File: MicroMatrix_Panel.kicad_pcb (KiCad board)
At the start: 2 copper layers, 86 x 36 mm, 385 parts

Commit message: Updated panel settings for fab
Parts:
- removed the REF** at (44.0, 43.2)
- removed the REF** at (49.4, 22.8)
- removed the REF** at (73.3, 43.2)
- removed the REF** at (66.0, 43.2)
- removed the REF** at (51.9, 43.2)
- removed the REF** at (20.0, 17.5) (x2)
- removed the REF** at (20.0, 48.5) (x2)
- removed the REF** at (96.0, 17.5) (x2)
- removed the REF** at (86.1, 22.8)
- removed the REF** at (66.0, 22.8)
- removed the REF** at (45.3, 22.8)
- removed the REF** at (89.3, 22.8)
- removed the REF** at (42.1, 22.8)
- removed the REF** at (71.4, 22.8)
- removed the REF** at (71.4, 43.2)
- removed the REF** at (94.7, 43.2)
- removed the REF** at (48.7, 43.2)
- removed the REF** at (44.6, 43.2)
- removed the REF** at (73.9, 43.2)
- removed the REF** at (28.0, 22.8)
- removed the REF** at (73.3, 22.8)
- removed the REF** at (27.4, 22.8)
- removed the REF** at (20.7, 43.2)
- removed the REF** at (42.7, 22.8)
- removed the REF** at (21.3, 43.2)
- removed the REF** at (22.6, 43.2)
- removed the REF** at (88.6, 43.2)
- removed the REF** at (42.7, 43.2)
- removed the REF** at (43.3, 43.2)
- removed the REF** at (45.3, 43.2)
- removed the REF** at (72.7, 22.8)
- removed the REF** at (44.6, 22.8)
- removed the REF** at (29.9, 22.8)
- removed the REF** at (64.7, 43.2)
- removed the REF** at (28.0, 43.2)
- removed the REF** at (51.3, 43.2)
- removed the REF** at (70.7, 43.2)
- removed the REF** at (67.3, 22.8)
- removed the REF** at (22.0, 43.2)
- removed the REF** at (28.7, 22.8)
- removed the REF** at (92.7, 22.8)
- removed the REF** at (67.3, 43.2)
- removed the REF** at (20.7, 22.8)
- removed the REF** at (22.0, 22.8)
- removed the REF** at (64.1, 22.8)
- removed the REF** at (26.7, 43.2)
- removed the REF** at (94.0, 22.8)
- removed the REF** at (88.6, 22.8)
- removed the REF** at (50.7, 43.2)
- removed the REF** at (95.9, 22.8)
- removed the REF** at (23.3, 43.2)
- removed the REF** at (64.1, 43.2)
- removed the REF** at (86.7, 43.2)
- removed the REF** at (28.7, 43.2)
- removed the REF** at (65.3, 22.8)
- removed the REF** at (20.1, 22.8)
- removed the REF** at (64.7, 22.8)
- removed the REF** at (95.9, 43.2)
- removed the REF** at (27.4, 43.2)
- removed the REF** at (66.6, 43.2)
- removed the REF** at (49.4, 43.2)
- removed the REF** at (23.3, 22.8)
- removed the REF** at (88.0, 22.8)
- removed the REF** at (93.4, 22.8)
- removed the REF** at (72.0, 22.8)
- removed the REF** at (29.9, 43.2)
- removed the REF** at (92.7, 43.2)
- removed the REF** at (50.0, 22.8)
- removed the REF** at (87.3, 43.2)
- removed the REF** at (51.3, 22.8)
- removed the REF** at (88.0, 43.2)
- removed the REF** at (87.3, 22.8)
- removed the REF** at (95.3, 22.8)
- removed the REF** at (29.3, 43.2)
- removed the REF** at (72.0, 43.2)
- removed the REF** at (95.3, 43.2)
- removed the REF** at (73.9, 22.8)
- removed the REF** at (66.6, 22.8)
- removed the REF** at (44.0, 22.8)
- removed the REF** at (70.7, 22.8)
- removed the REF** at (50.7, 22.8)
- removed the REF** at (22.6, 22.8)
- removed the REF** at (72.7, 43.2)
- removed the REF** at (86.7, 22.8)
- removed the REF** at (26.7, 22.8)
- removed the REF** at (20.1, 43.2)
- removed the REF** at (48.7, 22.8)
- removed the REF** at (42.1, 43.2)
- removed the REF** at (86.1, 43.2)
- removed the REF** at (51.9, 22.8)
- removed the REF** at (43.3, 22.8)
- removed the REF** at (94.7, 22.8)
- removed the REF** at (89.3, 43.2)
- removed the REF** at (65.3, 43.2)
- removed the REF** at (21.3, 22.8)
- removed the REF** at (29.3, 22.8)
- removed the REF** at (94.0, 43.2)
- removed the REF** at (93.4, 43.2)
- removed the REF** at (50.0, 43.2)
- added REF**: NPTH, NPTH, F.Cu at (95.8, 43.3)
- added REF**: Fiducial, Fiducial, F.Cu at (96.0, 17.5)
- added REF**: NPTH, NPTH, F.Cu at (95.8, 22.7)
- added REF**: NPTH, NPTH, F.Cu at (26.8, 22.7)
- added REF**: NPTH, NPTH, F.Cu at (49.8, 43.3)
- added REF**: NPTH, NPTH, F.Cu at (27.8, 22.7)
- added REF**: NPTH, NPTH, F.Cu at (94.8, 22.7)
- added REF**: NPTH, NPTH, F.Cu at (49.8, 22.7)
- added REF**: NPTH, NPTH, F.Cu at (66.2, 43.3)
- added REF**: NPTH, NPTH, F.Cu at (22.2, 43.3)
- added REF**: NPTH, NPTH, F.Cu at (71.8, 22.7)
- added REF**: NPTH, NPTH, F.Cu at (23.2, 43.3)
- added REF**: NPTH, NPTH, F.Cu at (65.2, 43.3)
- added REF**: NPTH, NPTH, F.Cu at (64.2, 43.3)
- added REF**: NPTH, NPTH, F.Cu at (86.2, 43.3)
- added REF**: NPTH, NPTH, F.Cu at (45.2, 43.3)
- added REF**: NPTH, NPTH, F.Cu at (23.2, 22.7)
- added REF**: NPTH, NPTH, F.Cu at (20.2, 22.7)
- added REF**: NPTH, NPTH, F.Cu at (73.8, 43.3)
- added REF**: NPTH, NPTH, F.Cu at (20.2, 43.3)
- added REF**: NPTH, NPTH, F.Cu at (89.2, 22.7)
- added REF**: NPTH, NPTH, F.Cu at (28.8, 43.3)
- added REF**: NPTH, NPTH, F.Cu at (44.2, 43.3)
- added REF**: NPTH, NPTH, F.Cu at (87.2, 43.3)
- added REF**: NPTH, NPTH, F.Cu at (72.8, 43.3)
- added REF**: NPTH, NPTH, F.Cu at (29.8, 22.7)
- added REF**: NPTH, NPTH, F.Cu at (88.2, 43.3)
- added REF**: NPTH, NPTH, F.Cu at (51.8, 22.7)
- added REF**: NPTH, NPTH, F.Cu at (50.8, 22.7)
- added REF**: NPTH, NPTH, F.Cu at (21.2, 43.3)
- added REF**: NPTH, NPTH, F.Cu at (92.8, 43.3)
- added REF**: NPTH, NPTH, F.Cu at (67.2, 43.3)
- added REF**: NPTH, NPTH, F.Cu at (93.8, 22.7)
- added REF**: NPTH, NPTH, F.Cu at (48.8, 43.3)
- added REF**: NPTH, NPTH, F.Cu at (65.2, 22.7)
- added REF**: NPTH, NPTH, F.Cu at (88.2, 22.7)
- added REF**: NPTH, NPTH, F.Cu at (64.2, 22.7)
- added REF**: NPTH, NPTH, F.Cu at (43.2, 43.3)
- added REF**: NPTH, NPTH, F.Cu at (45.2, 22.7)
- added REF**: NPTH, NPTH, F.Cu at (70.8, 22.7)
- added REF**: NPTH, NPTH, F.Cu at (48.8, 22.7)
- added REF**: NPTH, NPTH, F.Cu at (44.2, 22.7)
- added REF**: Fiducial, Fiducial, F.Cu at (20.0, 17.5)
- added REF**: NPTH, NPTH, F.Cu at (27.8, 43.3)
- added REF**: NPTH, NPTH, F.Cu at (28.8, 22.7)
- added REF**: NPTH, NPTH, F.Cu at (67.2, 22.7)
- added REF**: NPTH, NPTH, F.Cu at (22.2, 22.7)
- added REF**: Fiducial, Fiducial, F.Cu at (20.0, 48.5)
- added REF**: NPTH, NPTH, F.Cu at (86.2, 22.7)
- added REF**: NPTH, NPTH, F.Cu at (66.2, 22.7)
- added REF**: NPTH, NPTH, F.Cu at (94.8, 43.3)
- added REF**: NPTH, NPTH, F.Cu at (89.2, 43.3)
- added REF**: NPTH, NPTH, F.Cu at (50.8, 43.3)
- added REF**: NPTH, NPTH, F.Cu at (29.8, 43.3)
- added REF**: NPTH, NPTH, F.Cu at (42.2, 43.3)
- added REF**: NPTH, NPTH, F.Cu at (72.8, 22.7)
- added REF**: NPTH, NPTH, F.Cu at (71.8, 43.3)
- added REF**: NPTH, NPTH, F.Cu at (51.8, 43.3)
- added REF**: NPTH, NPTH, F.Cu at (42.2, 22.7)
- added REF**: NPTH, NPTH, F.Cu at (21.2, 22.7)
- added REF**: NPTH, NPTH, F.Cu at (93.8, 43.3)
- added REF**: NPTH, NPTH, F.Cu at (70.8, 43.3)
- added REF**: NPTH, NPTH, F.Cu at (87.2, 22.7)
- added REF**: NPTH, NPTH, F.Cu at (92.8, 22.7)
- added REF**: NPTH, NPTH, F.Cu at (43.2, 22.7)
- added REF**: Fiducial, Fiducial, B.Cu at (96.0, 17.5)
- added REF**: Fiducial, Fiducial, B.Cu at (20.0, 17.5)
- added REF**: Fiducial, Fiducial, B.Cu at (20.0, 48.5)
- added REF**: NPTH, NPTH, F.Cu at (26.8, 43.3)
- added REF**: NPTH, NPTH, F.Cu at (73.8, 22.7)
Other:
- outline, holes or cut-outs redrawn
- board text added: "JLCJLCJLCJLC - REV${REVISION} - ${ISSUE_DATE}"
- board text removed: "JLCJLCJLCJLC - ${REVISION} - ${ISSUE_DATE}"

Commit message: Updated Panel PCB to REV1.2
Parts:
- removed the D25 at (100.0, 31.4)
- removed the D25 at (56.0, 31.4)
- removed the D25 at (78.0, 31.4)
- removed the D25 at (34.0, 31.4)
- removed the D26 at (31.5, 31.4)
- removed the D26 at (53.5, 31.4)
- removed the D26 at (97.5, 31.4)
- removed the D26 at (75.5, 31.4)
- removed the D27 at (29.0, 31.4)
- removed the D27 at (95.0, 31.4)
- removed the D27 at (73.0, 31.4)
- removed the D27 at (51.0, 31.4)
- removed the D28 at (48.5, 31.4)
- removed the D28 at (26.5, 31.4)
- removed the D28 at (70.5, 31.4)
- removed the D28 at (92.5, 31.4)
- removed the D29 at (46.0, 31.4)
- removed the D29 at (24.0, 31.4)
- removed the D29 at (68.0, 31.4)
- removed the D29 at (90.0, 31.4)
- removed the D30 at (43.5, 31.4)
- removed the D30 at (21.5, 31.4)
- removed the D30 at (65.5, 31.4)
- removed the D30 at (87.5, 31.4)
- removed the D31 at (85.0, 31.4)
- removed the D31 at (19.0, 31.4)
- removed the D31 at (63.0, 31.4)
- removed the D31 at (41.0, 31.4)
- removed the D32 at (38.5, 31.4)
- removed the D32 at (60.5, 31.4)
- removed the D32 at (16.5, 31.4)
- removed the D32 at (82.5, 31.4)
- removed the REF** at (95.8, 43.3)
- removed the REF** at (96.0, 17.5) (x2)
- removed the REF** at (95.8, 22.7)
- removed the REF** at (26.8, 22.7)
- removed the REF** at (49.8, 43.3)
- removed the REF** at (27.8, 22.7)
- removed the REF** at (94.8, 22.7)
- removed the REF** at (49.8, 22.7)
- removed the REF** at (66.2, 43.3)
- removed the REF** at (22.2, 43.3)
- removed the REF** at (71.8, 22.7)
- removed the REF** at (23.2, 43.3)
- removed the REF** at (65.2, 43.3)
- removed the REF** at (64.2, 43.3)
- removed the REF** at (86.2, 43.3)
- removed the REF** at (45.2, 43.3)
- removed the REF** at (23.2, 22.7)
- removed the REF** at (20.2, 22.7)
- removed the REF** at (73.8, 43.3)
- removed the REF** at (20.2, 43.3)
- removed the REF** at (89.2, 22.7)
- removed the REF** at (28.8, 43.3)
- removed the REF** at (44.2, 43.3)
- removed the REF** at (87.2, 43.3)
- removed the REF** at (72.8, 43.3)
- removed the REF** at (29.8, 22.7)
- removed the REF** at (88.2, 43.3)
- removed the REF** at (51.8, 22.7)
- removed the REF** at (50.8, 22.7)
- removed the REF** at (21.2, 43.3)
- removed the REF** at (92.8, 43.3)
- removed the REF** at (67.2, 43.3)
- removed the REF** at (93.8, 22.7)
- removed the REF** at (48.8, 43.3)
- removed the REF** at (65.2, 22.7)
- removed the REF** at (88.2, 22.7)
- removed the REF** at (64.2, 22.7)
- removed the REF** at (43.2, 43.3)
- removed the REF** at (45.2, 22.7)
- removed the REF** at (70.8, 22.7)
- removed the REF** at (48.8, 22.7)
- removed the REF** at (44.2, 22.7)
- removed the REF** at (20.0, 17.5) (x2)
- removed the REF** at (27.8, 43.3)
- removed the REF** at (28.8, 22.7)
- removed the REF** at (67.2, 22.7)
- removed the REF** at (22.2, 22.7)
- removed the REF** at (20.0, 48.5) (x2)
- removed the REF** at (86.2, 22.7)
- removed the REF** at (66.2, 22.7)
- removed the REF** at (94.8, 43.3)
- removed the REF** at (89.2, 43.3)
- removed the REF** at (50.8, 43.3)
- removed the REF** at (29.8, 43.3)
- removed the REF** at (42.2, 43.3)
- removed the REF** at (72.8, 22.7)
- removed the REF** at (71.8, 43.3)
- removed the REF** at (51.8, 43.3)
- removed the REF** at (42.2, 22.7)
- removed the REF** at (21.2, 22.7)
- removed the REF** at (93.8, 43.3)
- removed the REF** at (70.8, 43.3)
- removed the REF** at (87.2, 22.7)
- removed the REF** at (92.8, 22.7)
- removed the REF** at (43.2, 22.7)
- removed the REF** at (26.8, 43.3)
- removed the REF** at (73.8, 22.7)
- added D25: SK6805, LED_SMD:LED_SK6812_EC15_1.5x1.5mm, F.Cu at (56.0, 31.5)
- added D25: SK6805, LED_SMD:LED_SK6812_EC15_1.5x1.5mm, F.Cu at (34.0, 31.5)
- added D25: SK6805, LED_SMD:LED_SK6812_EC15_1.5x1.5mm, F.Cu at (100.0, 31.5)
- added D25: SK6805, LED_SMD:LED_SK6812_EC15_1.5x1.5mm, F.Cu at (78.0, 31.5)
- added D26: SK6805, LED_SMD:LED_SK6812_EC15_1.5x1.5mm, F.Cu at (53.5, 31.5)
- added D26: SK6805, LED_SMD:LED_SK6812_EC15_1.5x1.5mm, F.Cu at (31.5, 31.5)
- added D26: SK6805, LED_SMD:LED_SK6812_EC15_1.5x1.5mm, F.Cu at (97.5, 31.5)
- added D26: SK6805, LED_SMD:LED_SK6812_EC15_1.5x1.5mm, F.Cu at (75.5, 31.5)
- added D27: SK6805, LED_SMD:LED_SK6812_EC15_1.5x1.5mm, F.Cu at (95.0, 31.5)
- added D27: SK6805, LED_SMD:LED_SK6812_EC15_1.5x1.5mm, F.Cu at (51.0, 31.5)
- added D27: SK6805, LED_SMD:LED_SK6812_EC15_1.5x1.5mm, F.Cu at (73.0, 31.5)
- added D27: SK6805, LED_SMD:LED_SK6812_EC15_1.5x1.5mm, F.Cu at (29.0, 31.5)
- added D28: SK6805, LED_SMD:LED_SK6812_EC15_1.5x1.5mm, F.Cu at (26.5, 31.5)
- added D28: SK6805, LED_SMD:LED_SK6812_EC15_1.5x1.5mm, F.Cu at (92.5, 31.5)
- added D28: SK6805, LED_SMD:LED_SK6812_EC15_1.5x1.5mm, F.Cu at (70.5, 31.5)
- added D28: SK6805, LED_SMD:LED_SK6812_EC15_1.5x1.5mm, F.Cu at (48.5, 31.5)
- added D29: SK6805, LED_SMD:LED_SK6812_EC15_1.5x1.5mm, F.Cu at (90.0, 31.5)
- added D29: SK6805, LED_SMD:LED_SK6812_EC15_1.5x1.5mm, F.Cu at (46.0, 31.5)
- added D29: SK6805, LED_SMD:LED_SK6812_EC15_1.5x1.5mm, F.Cu at (68.0, 31.5)
- added D29: SK6805, LED_SMD:LED_SK6812_EC15_1.5x1.5mm, F.Cu at (24.0, 31.5)
- added D30: SK6805, LED_SMD:LED_SK6812_EC15_1.5x1.5mm, F.Cu at (87.5, 31.5)
- added D30: SK6805, LED_SMD:LED_SK6812_EC15_1.5x1.5mm, F.Cu at (21.5, 31.5)
- added D30: SK6805, LED_SMD:LED_SK6812_EC15_1.5x1.5mm, F.Cu at (65.5, 31.5)
- added D30: SK6805, LED_SMD:LED_SK6812_EC15_1.5x1.5mm, F.Cu at (43.5, 31.5)
- added D31: SK6805, LED_SMD:LED_SK6812_EC15_1.5x1.5mm, F.Cu at (85.0, 31.5)
- added D31: SK6805, LED_SMD:LED_SK6812_EC15_1.5x1.5mm, F.Cu at (19.0, 31.5)
- added D31: SK6805, LED_SMD:LED_SK6812_EC15_1.5x1.5mm, F.Cu at (41.0, 31.5)
- added D31: SK6805, LED_SMD:LED_SK6812_EC15_1.5x1.5mm, F.Cu at (63.0, 31.5)
- added D32: SK6805, LED_SMD:LED_SK6812_EC15_1.5x1.5mm, F.Cu at (16.5, 31.5)
- added D32: SK6805, LED_SMD:LED_SK6812_EC15_1.5x1.5mm, F.Cu at (82.5, 31.5)
- added D32: SK6805, LED_SMD:LED_SK6812_EC15_1.5x1.5mm, F.Cu at (60.5, 31.5)
- added D32: SK6805, LED_SMD:LED_SK6812_EC15_1.5x1.5mm, F.Cu at (38.5, 31.5)
- added REF**: NPTH, NPTH, F.Cu at (67.5, 22.7)
- added REF**: NPTH, NPTH, F.Cu at (91.5, 43.3)
- added REF**: NPTH, NPTH, F.Cu at (25.5, 43.3)
- added REF**: NPTH, NPTH, F.Cu at (67.5, 43.3)
- added REF**: NPTH, NPTH, F.Cu at (70.5, 22.7)
- added REF**: NPTH, NPTH, F.Cu at (46.5, 43.3)
- added REF**: NPTH, NPTH, F.Cu at (92.5, 22.7)
- added REF**: NPTH, NPTH, F.Cu at (90.5, 22.7)
- added REF**: NPTH, NPTH, F.Cu at (45.5, 22.7)
- added REF**: NPTH, NPTH, F.Cu at (46.5, 22.7)
- added REF**: NPTH, NPTH, F.Cu at (24.5, 43.3)
- added REF**: NPTH, NPTH, F.Cu at (68.5, 43.3)
- added REF**: Fiducial, Fiducial, F.Cu at (96.0, 17.5)
- added REF**: NPTH, NPTH, F.Cu at (48.5, 22.7)
- added REF**: NPTH, NPTH, F.Cu at (70.5, 43.3)
- added REF**: NPTH, NPTH, F.Cu at (45.5, 43.3)
- added REF**: NPTH, NPTH, F.Cu at (47.5, 22.7)
- added REF**: NPTH, NPTH, F.Cu at (69.5, 22.7)
- added REF**: NPTH, NPTH, F.Cu at (47.5, 43.3)
- added REF**: NPTH, NPTH, F.Cu at (23.5, 22.7)
- added REF**: Fiducial, Fiducial, F.Cu at (20.0, 48.5)
- added REF**: NPTH, NPTH, F.Cu at (89.5, 22.7)
- added REF**: NPTH, NPTH, F.Cu at (48.5, 43.3)
- added REF**: NPTH, NPTH, F.Cu at (91.5, 22.7)
- added REF**: NPTH, NPTH, F.Cu at (24.5, 22.7)
- added REF**: NPTH, NPTH, F.Cu at (90.5, 43.3)
- added REF**: NPTH, NPTH, F.Cu at (89.5, 43.3)
- added REF**: NPTH, NPTH, F.Cu at (69.5, 43.3)
- added REF**: NPTH, NPTH, F.Cu at (25.5, 22.7)
- added REF**: Fiducial, Fiducial, B.Cu at (20.0, 48.5)
- added REF**: NPTH, NPTH, F.Cu at (92.5, 43.3)
- added REF**: Fiducial, Fiducial, B.Cu at (96.0, 17.5)
- added REF**: Fiducial, Fiducial, B.Cu at (20.0, 17.5)
- added REF**: NPTH, NPTH, F.Cu at (23.5, 43.3)
- added REF**: NPTH, NPTH, F.Cu at (68.5, 22.7)
- added REF**: NPTH, NPTH, F.Cu at (26.5, 43.3)
- added REF**: Fiducial, Fiducial, F.Cu at (20.0, 17.5)
- added REF**: NPTH, NPTH, F.Cu at (26.5, 22.7)
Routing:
- net Board_3-+5V: track 159.2 -> 153.9 mm, vias 9 -> 8
- net Board_2-+5V: track 159.2 -> 153.9 mm, vias 9 -> 8
- net Board_1-+5V: track 159.2 -> 153.9 mm, vias 9 -> 8
- net Board_0-+5V: track 159.2 -> 153.9 mm, vias 9 -> 8
- net Board_0-DIN: track 14.0 -> 15.2 mm
- net Board_2-DIN: track 14.0 -> 15.2 mm
- net Board_1-DIN: track 14.0 -> 15.2 mm
- net Board_3-DIN: track 14.0 -> 15.2 mm
- net Board_3-GND: track 0.10 -> 0.00 mm, vias 33 -> 34
- net Board_2-GND: track 0.10 -> 0.00 mm, vias 33 -> 34
- net Board_1-GND: track 0.10 -> 0.00 mm, vias 33 -> 34
- net Board_0-GND: track 0.10 -> 0.00 mm, vias 33 -> 34
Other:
- outline, holes or cut-outs redrawn
- board text added: "REV1.2"
- board text removed: "REV1.1"

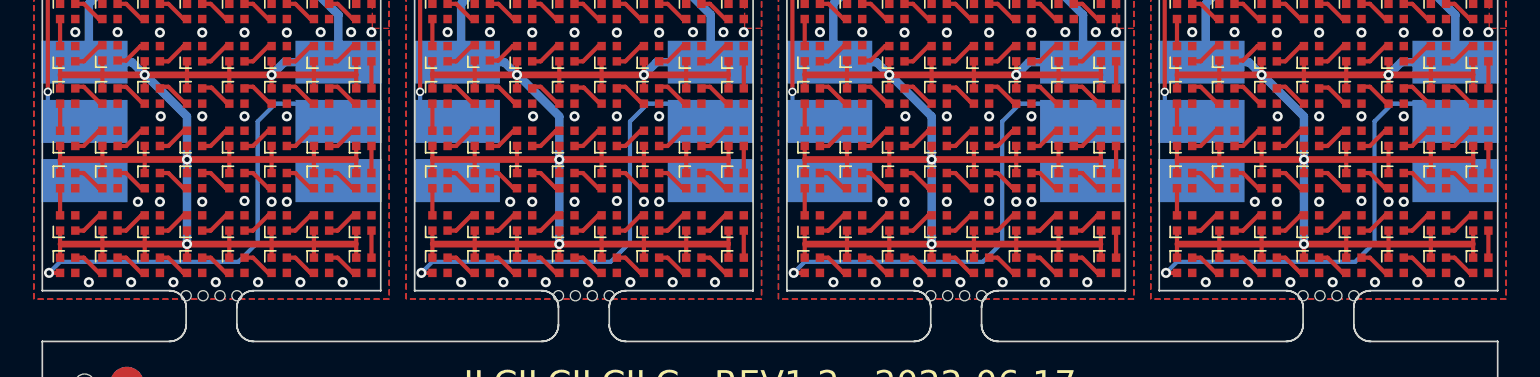
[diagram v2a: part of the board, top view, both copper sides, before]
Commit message: Fixed Trace in REV1.2
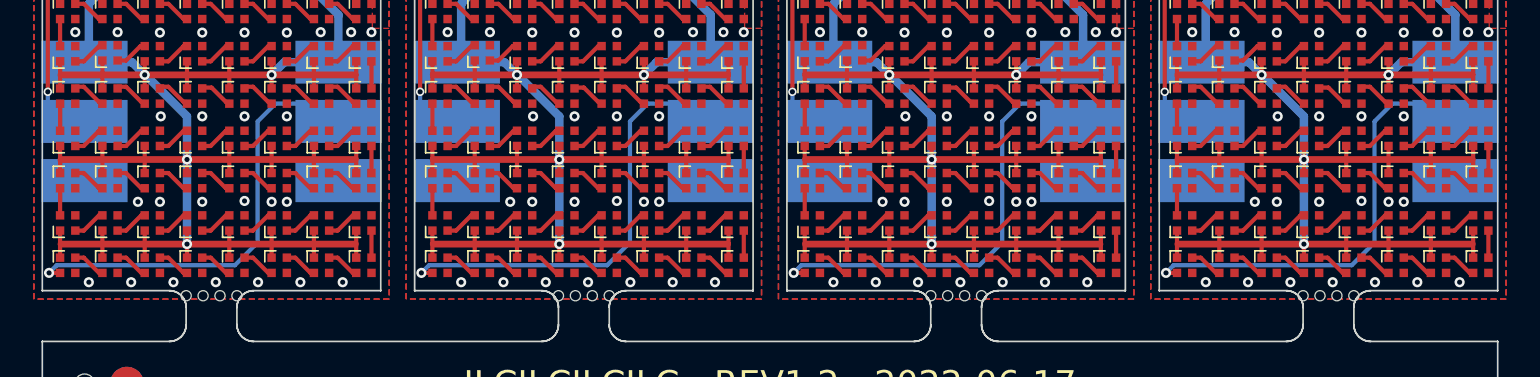
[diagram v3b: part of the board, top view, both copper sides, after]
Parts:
- removed the REF** at (96.0, 17.5) (x2)
- removed the REF** at (20.0, 48.5) (x2)
- removed the REF** at (20.0, 17.5) (x2)
- added REF**: Fiducial, Fiducial, F.Cu at (20.0, 17.5)
- added REF**: Fiducial, Fiducial, F.Cu at (96.0, 17.5)
- added REF**: Fiducial, Fiducial, F.Cu at (20.0, 48.5)
- added REF**: Fiducial, Fiducial, B.Cu at (20.0, 17.5)
- added REF**: Fiducial, Fiducial, B.Cu at (96.0, 17.5)
- added REF**: Fiducial, Fiducial, B.Cu at (20.0, 48.5)
